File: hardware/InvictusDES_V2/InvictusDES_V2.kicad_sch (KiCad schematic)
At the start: 76 parts, among them J1 Screw_Terminal_01x02, J10 USB_B_Micro, J11 Conn_01x06, J12 Micro_SD_Card, J2 Conn_02x05_Odd_Even, J3 Conn_01x03, J4 Conn_01x03, J5 Conn_01x03, J6 Conn_01x03, J7 Conn_01x03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

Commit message: updated PCB, pre-DRC, new IMU, all traces routed for now
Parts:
- removed J3, J4, J5, J6, J7, J8: Conn_01x03, Connector_PinHeader_2.54mm:PinHeader_1x03_P2.54mm_Vertical, symbol Connector_Generic:Conn_01x03
- removed R14: 1M, Resistor_SMD:R_0603_1608Metric, symbol Device:R
- removed R15: 100k, Resistor_SMD:R_0603_1608Metric, symbol Device:R
- added J3: Conn_01x06, Connector_JST:JST_SH_BM06B-SRSS-TB_1x06-1MP_P1.00mm_Vertical, symbol Connector_Generic:Conn_01x06
- added R16: 1.5k, Resistor_SMD:R_0603_1608Metric, symbol Device:R
- added R17, R18: 22, Resistor_SMD:R_0402_1005Metric, symbol Device:R
- added TP1, TP2, TP3, TP4, TP5, TP6: TestPoint, symbol Connector:TestPoint
- U1: footprint RDX0007A-MFG -> TPSM863257:RDX0007A-MFG
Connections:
- net +3V3: now also R16.2
- net GND: now also J12.9 (SHIELD)
- net SERVO_1: now also J3.1 (Pin_1)
- net SERVO_2: now also J3.2 (Pin_2)
- net SERVO_3: now also J3.3 (Pin_3)
- net SERVO_4: now also J3.4 (Pin_4)
- net SERVO_5: now also J3.5 (Pin_5)
- net SERVO_6: now also J3.6 (Pin_6)
- net SPI1_MISO: now also TP2.1
- net SPI1_MOSI: now also TP3.1
- net SPI1_SCK: now also TP1.1
- net SPI2_MISO: now also TP5.1
- net SPI2_MOSI: now also TP4.1
- net SPI2_SCK: now also TP6.1
- net USB_CONN_DM renamed USB_CONN_D-
- net USB_CONN_DP renamed USB_CONN_D+
- net USB_DM: no longer names the net of U2.44 (PA11)
- net USB_DM: now also R18.2; no longer U7.6 (I/O1)
- net USB_DP: no longer names the net of U2.45 (PA12)
- net USB_DP: now also R17.2; no longer U7.4 (I/O2)
- new net USB_D+: R16.1, R17.1, U7.4 (I/O2)
- new net USB_D-: R18.1, U7.6 (I/O1)
- no-connect marks 31 -> 30
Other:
- moved on the sheet: C14, C17, C19, C2, C20, C26, C27, C29, C6, D2, FB2, H1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

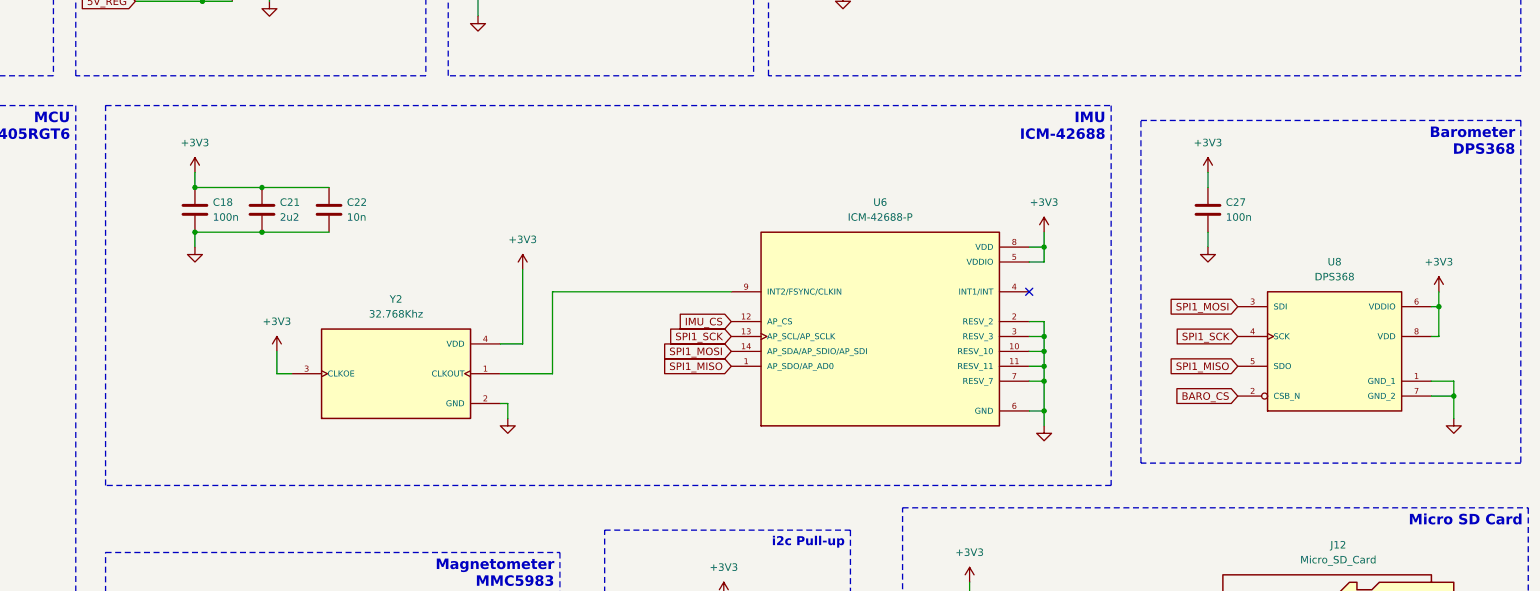
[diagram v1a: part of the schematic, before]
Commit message: Test Points, spi bus tidying, and fab prep
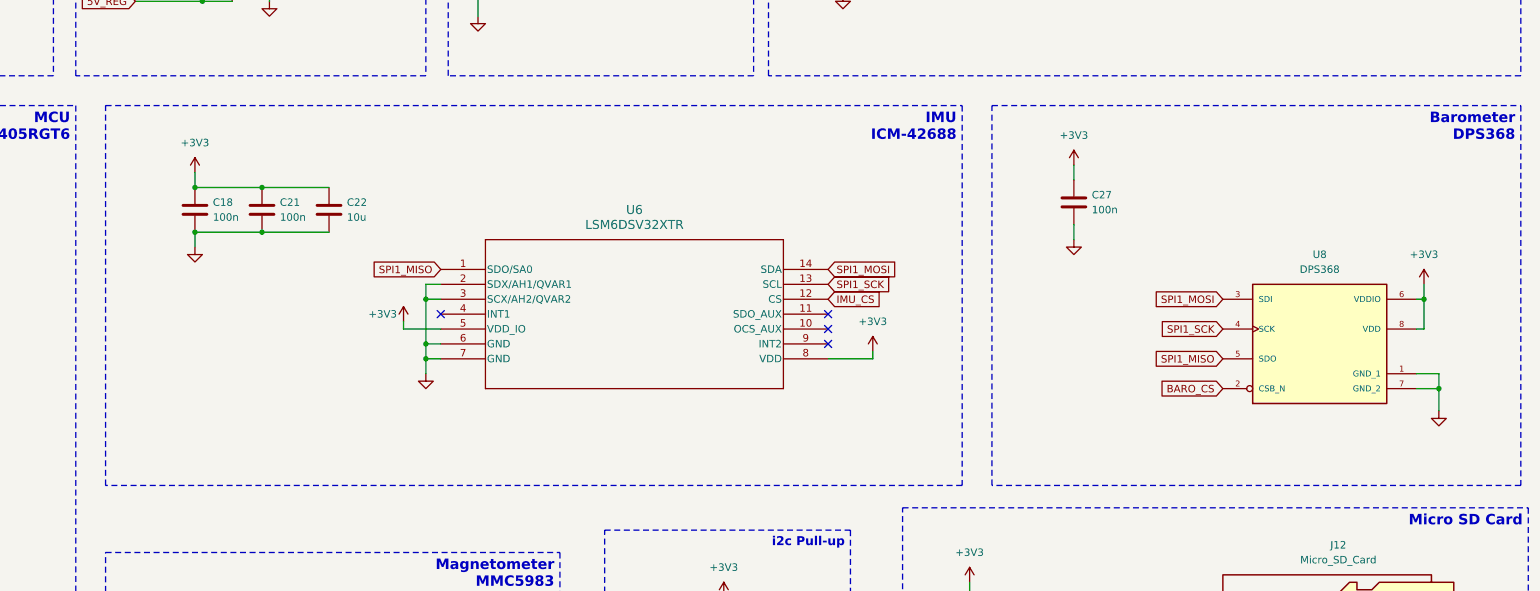
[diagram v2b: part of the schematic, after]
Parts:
- removed U6: ICM-42688-P, ICM-42688-P (3):PQFN50P300X250X97-14N, symbol ICM-42688-P:ICM-42688-P
- removed Y2: 32.768Khz, OV-7604-C7_32.768KHZ_20PPM_TA_QC:OSC_OV-7604-C7_32.768KHZ_20PPM_TA_QC, symbol OV-7604-C7_32.768KHZ_20PPM_TA_QC:OV-7604-C7_32.768KHZ_20PPM_TA_QC
- added U6: LSM6DSV32XTR, LSM6DSV32XTR:LGA-14L_2p5X3p0X0p86_STM, symbol LSM6DSV32XTR:LSM6DSV32XTR
- C21: value 2u2 -> 100n
- C22: value 10n -> 10u
- H1, H2, H3, H4: footprint MountingHole:MountingHole_3.5mm_Pad_Via -> MountingHole:MountingHole_2.2mm_M2
- TP1: footprint (none) -> TestPoint:TestPoint_Keystone_5000-5004_Miniature
- TP2, TP3, TP4, TP5, TP6: footprint (none) -> TestPoint:TestPoint_Pad_D1.0mm
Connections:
- net +3V3: now also U6.5 (VDD_IO), U6.8 (VDD)
- net GND: now also U6.2 (SDX/AH1/QVAR1), U6.3 (SCX/AH2/QVAR2), U6.6 (GND), U6.7 (GND)
- net IMU_CS: now also U6.12 (CS)
- net SPI1_MISO: now also U6.1 (SDO/SA0)
- net SPI1_MOSI: now also U6.14 (SDA)
- net SPI1_SCK: now also U6.13 (SCL)
- no-connect marks 30 -> 33
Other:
- moved on the sheet: C27, U8

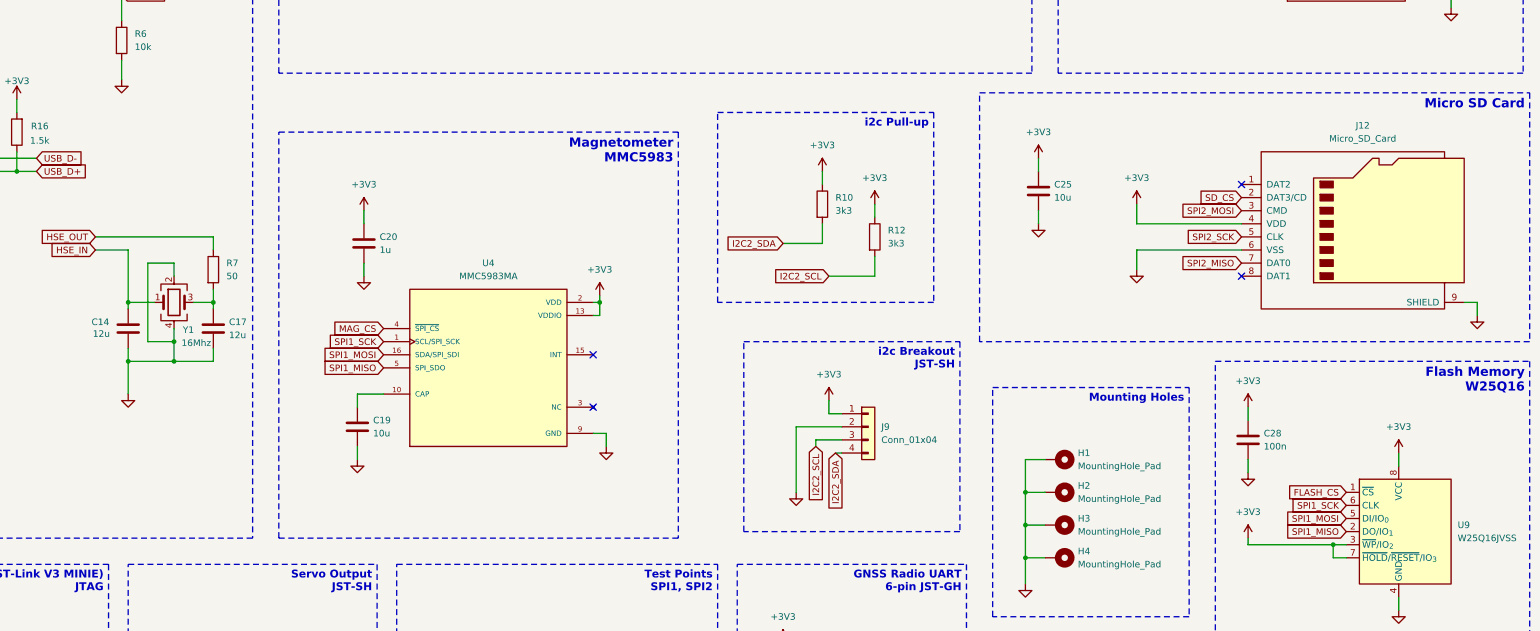
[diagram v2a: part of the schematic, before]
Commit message: new imu, organized GPIOs, new sensor layout
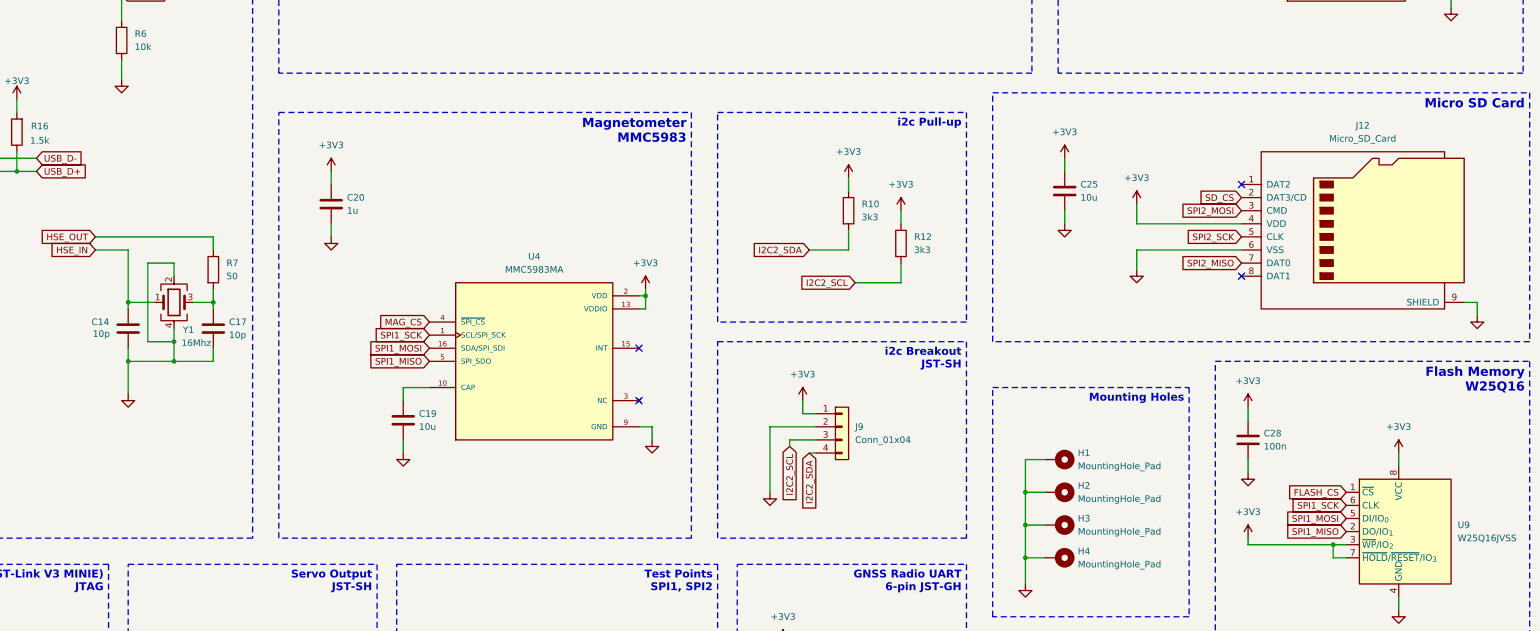
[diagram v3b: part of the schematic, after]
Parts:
- C14, C17: value 12u -> 10p
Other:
- moved on the sheet: C19, C20, C25, J9, R10, R12, U4

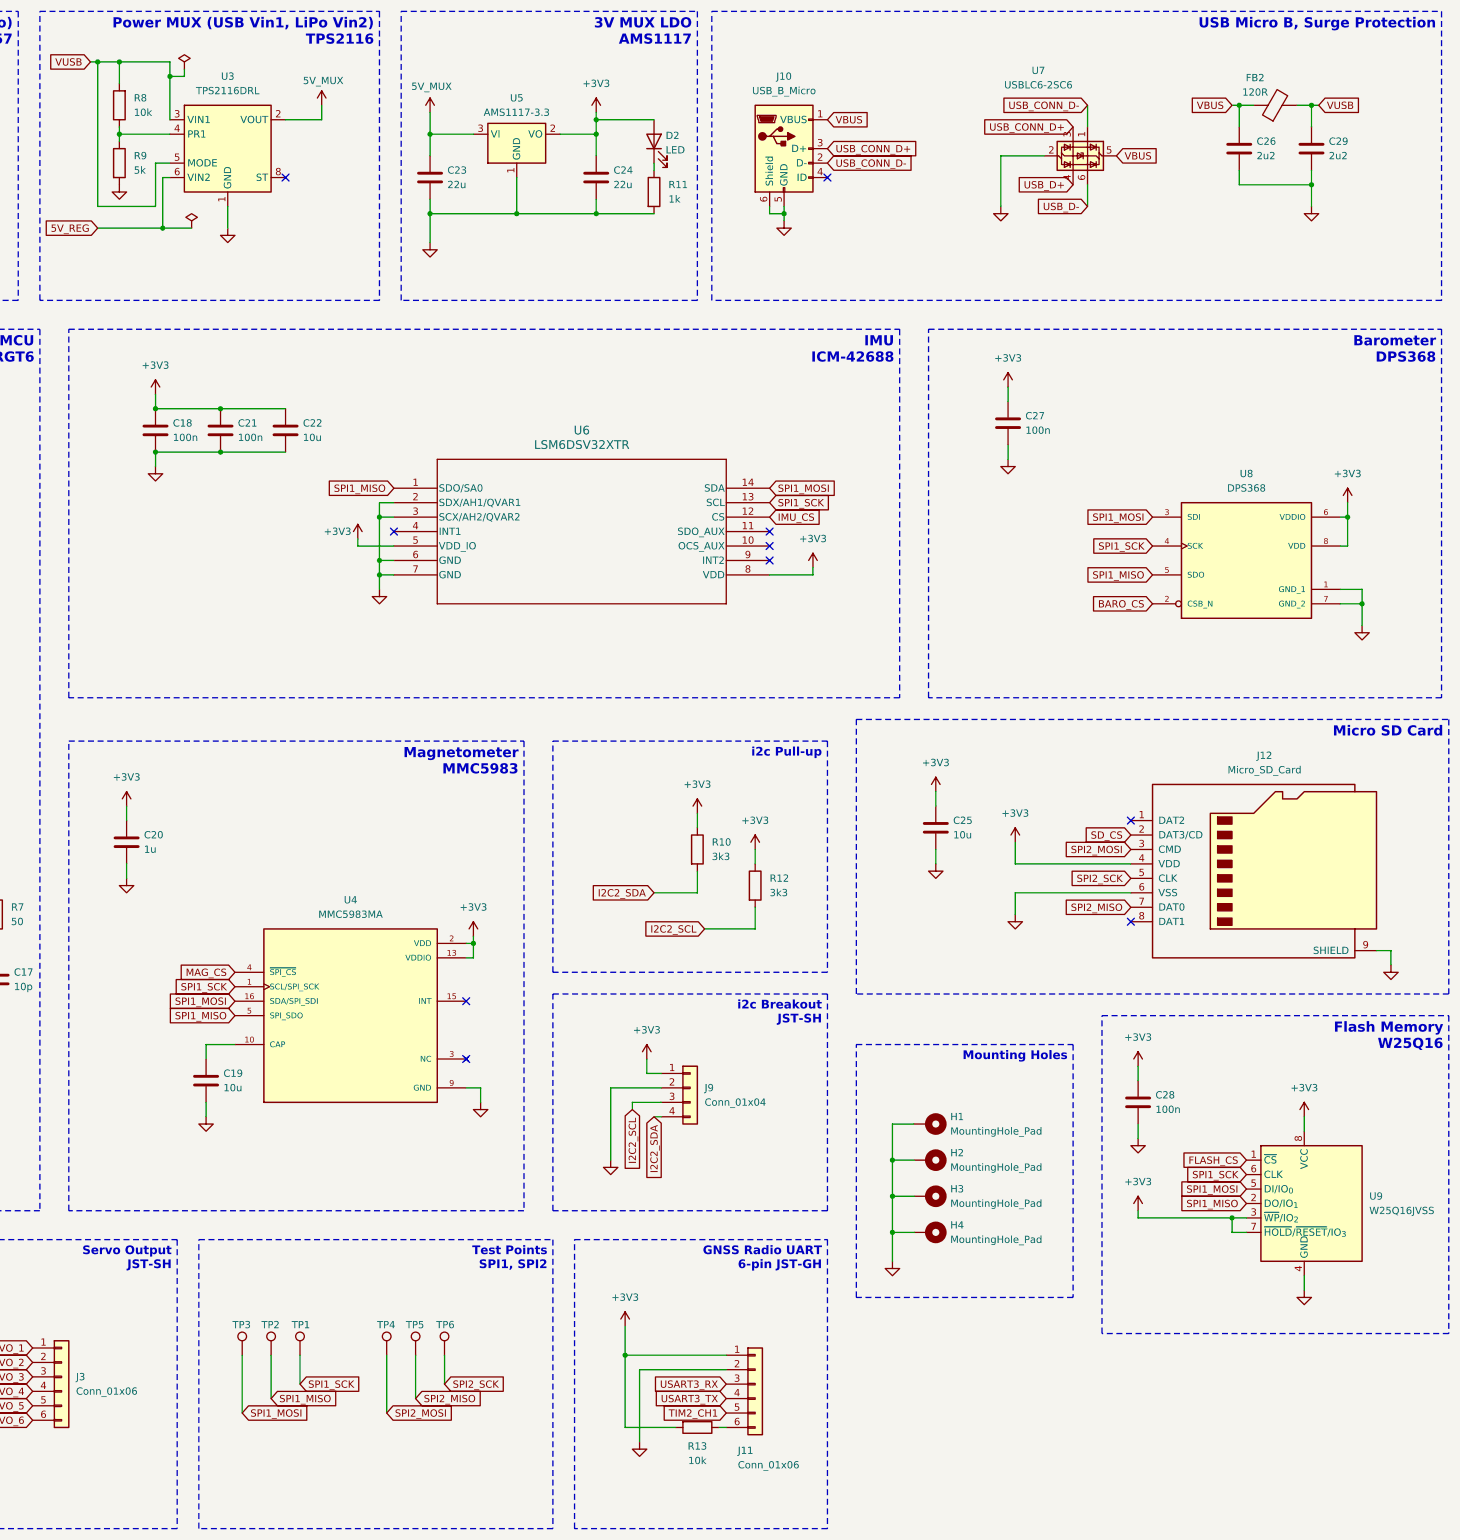
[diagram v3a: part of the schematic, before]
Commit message: Adjusted i2c, GPIO breakouts, DRC-passed
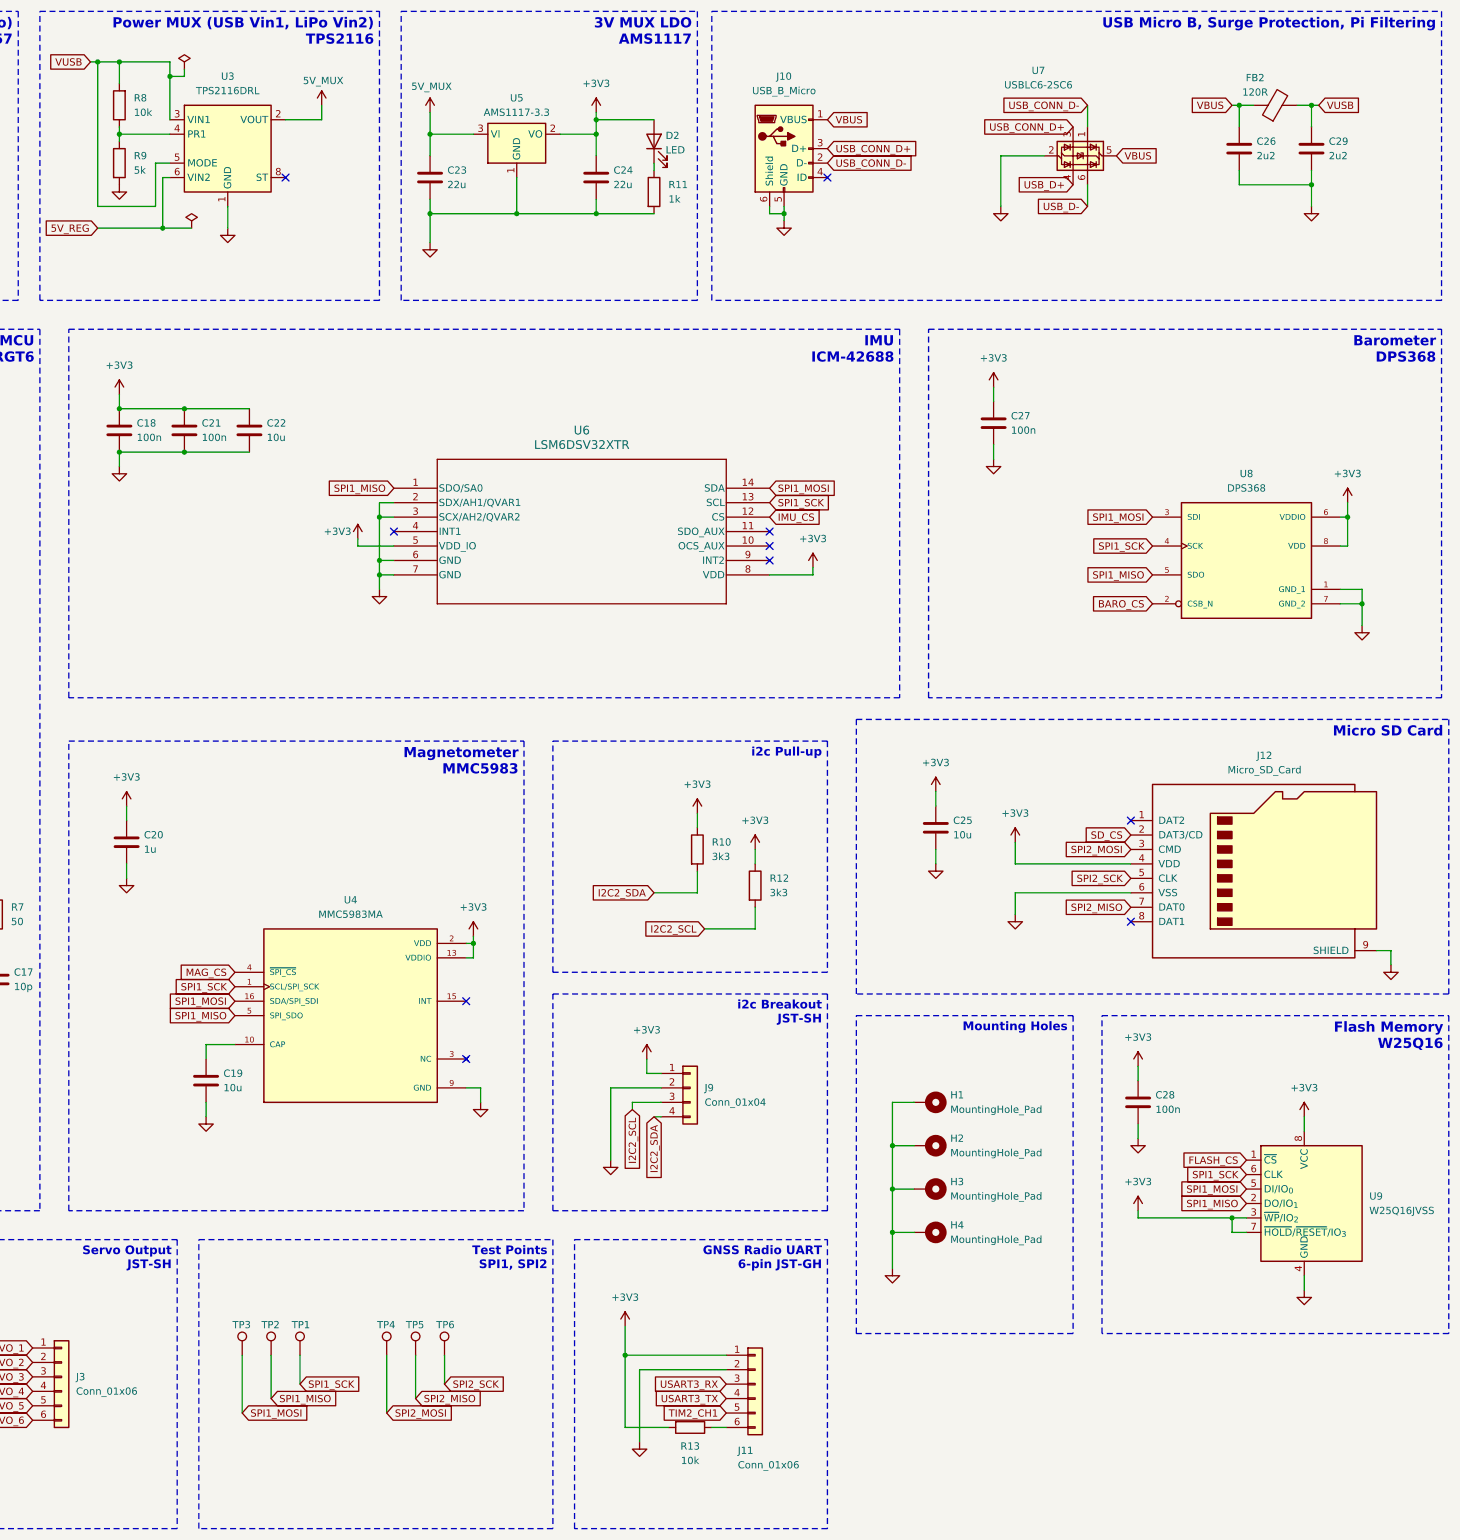
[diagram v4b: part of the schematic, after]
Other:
- moved on the sheet: C18, C21, C22, C27, H1, H2, H3, R13

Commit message: Connectors made to JST-SH, aligned silkscreen designators and connectors
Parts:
- J11: footprint Connector_Molex:Molex_PicoBlade_53047-0610_1x06_P1.25mm_Vertical -> Connector_JST:JST_SH_BM06B-SRSS-TB_1x06-1MP_P1.00mm_Vertical
- J9: footprint Connector_Molex:Molex_PicoBlade_53047-0410_1x04_P1.25mm_Vertical -> Connector_JST:JST_SH_BM04B-SRSS-TB_1x04-1MP_P1.00mm_Vertical
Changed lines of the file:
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@@
 			)
 		)
-		(property "Footprint" "Connector_Molex:Molex_PicoBlade_53047-0610_1x06_P1.25mm_Vertical"
+		(property "Footprint" "Connector_JST:JST_SH_BM06B-SRSS-TB_1x06-1MP_P1.00mm_Vertical"
 			(at 283.21 257.81 0)
 			(effects
@@
 			)
 		)
-		(property "Footprint" "Connector_Molex:Molex_PicoBlade_53047-0410_1x04_P1.25mm_Vertical"
+		(property "Footprint" "Connector_JST:JST_SH_BM04B-SRSS-TB_1x04-1MP_P1.00mm_Vertical"
 			(at 271.78 205.74 0)
 			(effects
